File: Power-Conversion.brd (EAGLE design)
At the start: 182.9 x 114.3 mm, 50 parts, among them Q1 SUM90P10-19L, U7 LM2678

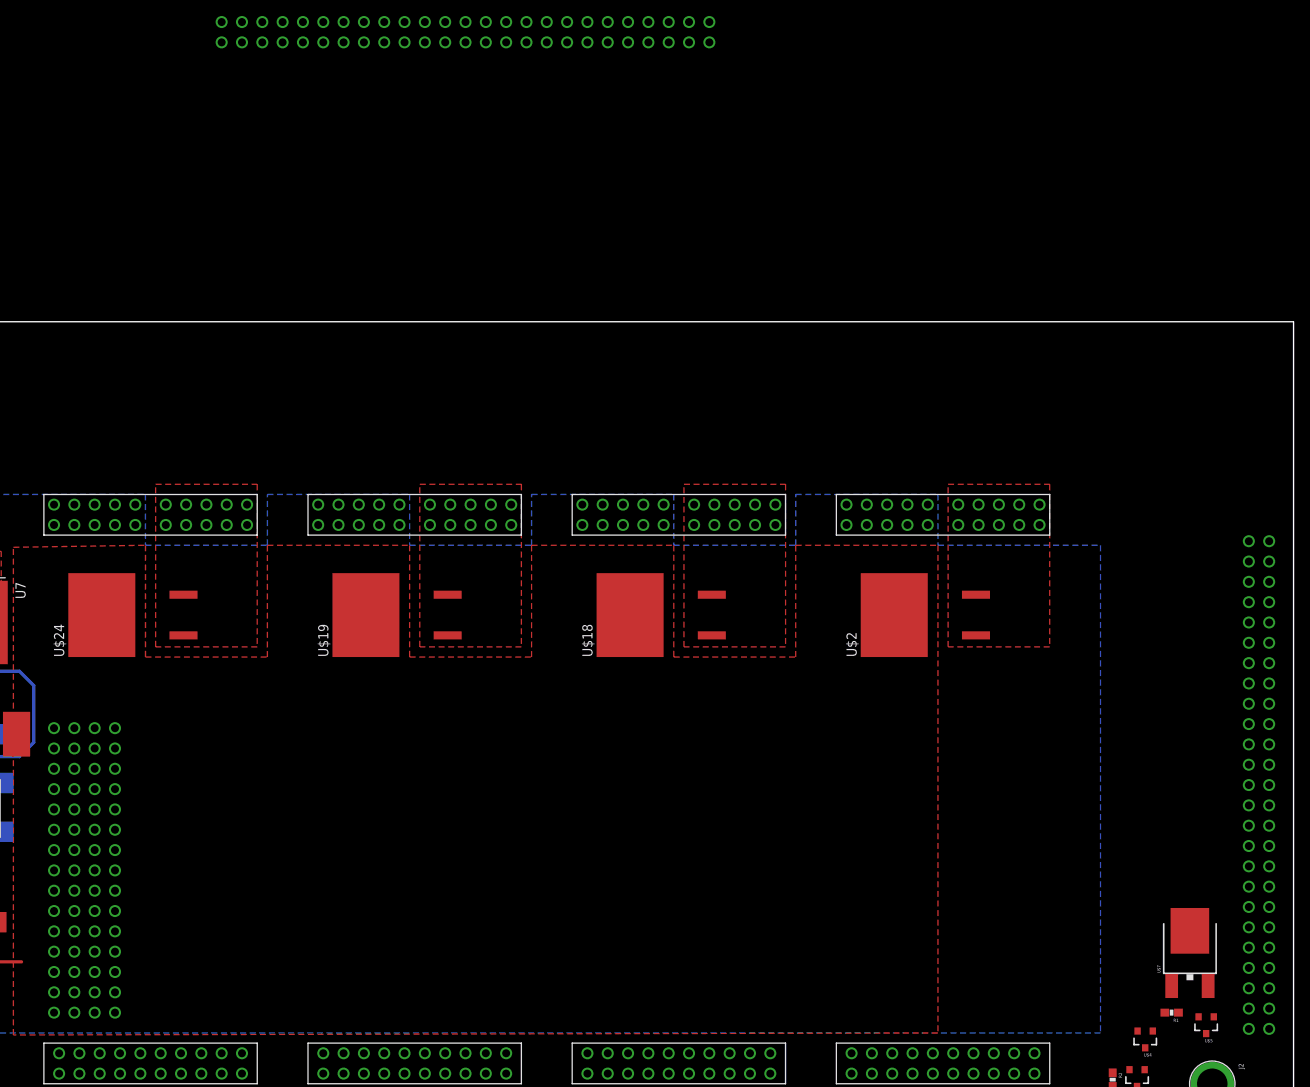
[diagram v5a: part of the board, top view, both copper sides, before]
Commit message: Added standard ESC board connector
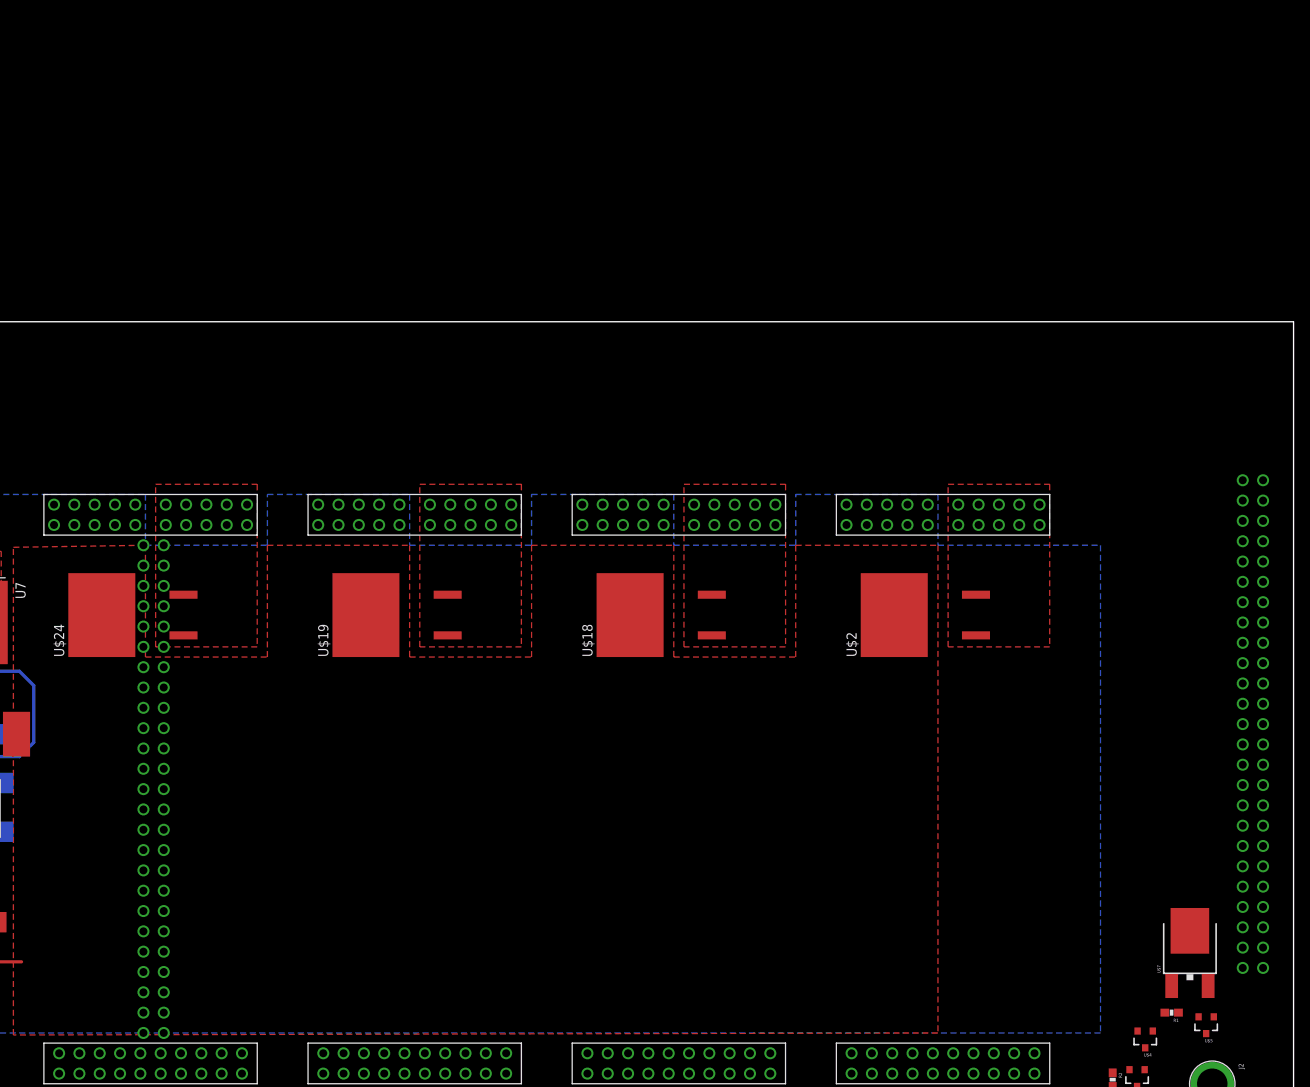
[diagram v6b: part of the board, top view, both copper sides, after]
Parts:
- removed U$13, U$14: POWER_BRICK_CONNECTORS(2X15), MotherBoardParts2:POWER_BRICK_CONNECTORS(2X15)
- removed U$3, U$8: POWER-BRICK-CONNECTOR, MotherboardParts:POWER-BRICK-CONNECTOR
- added U$17: ESC-CONNECTORESC-CONNECTOR, MotherboardParts:ESC-CONNECTOR
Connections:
- net +12V: now also U$17.P$100, U$17.P$51, U$17.P$52, U$17.P$53, U$17.P$54, U$17.P$55, U$17.P$56, U$17.P$57, U$17.P$58, U$17.P$59, U$17.P$60, U$17.P$61, U$17.P$62, U$17.P$63, U$17.P$64, U$17.P$65, U$17.P$66, U$17.P$67, U$17.P$68, U$17.P$69, U$17.P$70, U$17.P$71, U$17.P$72, U$17.P$73, U$17.P$74, U$17.P$75, U$17.P$76, U$17.P$77, U$17.P$78, U$17.P$79, U$17.P$80, U$17.P$81, U$17.P$82, U$17.P$83, U$17.P$84, U$17.P$85, U$17.P$86, U$17.P$87, U$17.P$88, U$17.P$89, U$17.P$90, U$17.P$91, U$17.P$92, U$17.P$93, U$17.P$94, U$17.P$95, U$17.P$96, U$17.P$97, U$17.P$98, U$17.P$99; no longer U$8.P$1, U$8.P$10, U$8.P$11, U$8.P$12, U$8.P$13, U$8.P$14, U$8.P$15, U$8.P$16, U$8.P$17, U$8.P$18, U$8.P$19, U$8.P$2, U$8.P$20, U$8.P$21, U$8.P$22, U$8.P$23, U$8.P$24, U$8.P$25, U$8.P$26, U$8.P$27, U$8.P$28, U$8.P$29, U$8.P$3, U$8.P$30, U$8.P$31, U$8.P$32, U$8.P$33, U$8.P$34, U$8.P$35, U$8.P$36, U$8.P$37, U$8.P$38, U$8.P$39, U$8.P$4, U$8.P$40, U$8.P$41, U$8.P$42, U$8.P$43, U$8.P$44, U$8.P$45, U$8.P$46, U$8.P$47, U$8.P$48, U$8.P$49, U$8.P$5, U$8.P$50, U$8.P$6, U$8.P$7, U$8.P$8, U$8.P$9
- net GND: now also U$17.P$1, U$17.P$10, U$17.P$11, U$17.P$12, U$17.P$13, U$17.P$14, U$17.P$15, U$17.P$16, U$17.P$17, U$17.P$18, U$17.P$19, U$17.P$2, U$17.P$20, U$17.P$21, U$17.P$22, U$17.P$23, U$17.P$24, U$17.P$25, U$17.P$26, U$17.P$27, U$17.P$28, U$17.P$29, U$17.P$3, U$17.P$30, U$17.P$31, U$17.P$32, U$17.P$33, U$17.P$34, U$17.P$35, U$17.P$36, U$17.P$37, U$17.P$38, U$17.P$39, U$17.P$4, U$17.P$40, U$17.P$41, U$17.P$42, U$17.P$43, U$17.P$44, U$17.P$45, U$17.P$46, U$17.P$47, U$17.P$48, U$17.P$49, U$17.P$5, U$17.P$50, U$17.P$6, U$17.P$7, U$17.P$8, U$17.P$9; no longer U$3.P$1, U$3.P$10, U$3.P$11, U$3.P$12, U$3.P$13, U$3.P$14, U$3.P$15, U$3.P$16, U$3.P$17, U$3.P$18, U$3.P$19, U$3.P$2, U$3.P$20, U$3.P$21, U$3.P$22, U$3.P$23, U$3.P$24, U$3.P$25, U$3.P$26, U$3.P$27, U$3.P$28, U$3.P$29, U$3.P$3, U$3.P$30, U$3.P$31, U$3.P$32, U$3.P$33, U$3.P$34, U$3.P$35, U$3.P$36, U$3.P$37, U$3.P$38, U$3.P$39, U$3.P$4, U$3.P$40, U$3.P$41, U$3.P$42, U$3.P$43, U$3.P$44, U$3.P$45, U$3.P$46, U$3.P$47, U$3.P$48, U$3.P$49, U$3.P$5, U$3.P$50, U$3.P$6, U$3.P$7, U$3.P$8, U$3.P$9

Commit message: Some routing done
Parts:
- U$17: value ESC-CONNECTORESC-CONNECTOR -> ESC-CONNECTORPARALLELL; device MotherboardParts:ESC-CONNECTOR -> MotherboardParts:ESC-PARALLELL
- turned R5 to 180 degrees
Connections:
- removed net SCL4: U$23.SCL
- removed net SDA4: U$23.SDA
- net +12V: now also U$17.P$101, U$17.P$102, U$17.P$103, U$17.P$104, U$17.P$105, U$17.P$106, U$17.P$107, U$17.P$108, U$17.P$109, U$17.P$110, U$17.P$111, U$17.P$112, U$17.P$113, U$17.P$114, U$17.P$115, U$17.P$116, U$17.P$117, U$17.P$118, U$17.P$119, U$17.P$120, U$17.P$121, U$17.P$122, U$17.P$123, U$17.P$124, U$17.P$125, U$17.P$126, U$17.P$127, U$17.P$128, U$17.P$129, U$17.P$130; no longer U$17.P$100, U$17.P$81, U$17.P$82, U$17.P$83, U$17.P$84, U$17.P$85, U$17.P$86, U$17.P$87, U$17.P$88, U$17.P$89, U$17.P$90, U$17.P$91, U$17.P$92, U$17.P$93, U$17.P$94, U$17.P$95, U$17.P$96, U$17.P$97, U$17.P$98, U$17.P$99
- net SCL1: now also U$23.SCL
- net SDA1: now also U$23.SDA
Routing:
- net GND: track 19.7 -> 33.1 mm
- net SDA: track 0.00 -> 5.31 mm
- net SCL: track 0.00 -> 5.29 mm

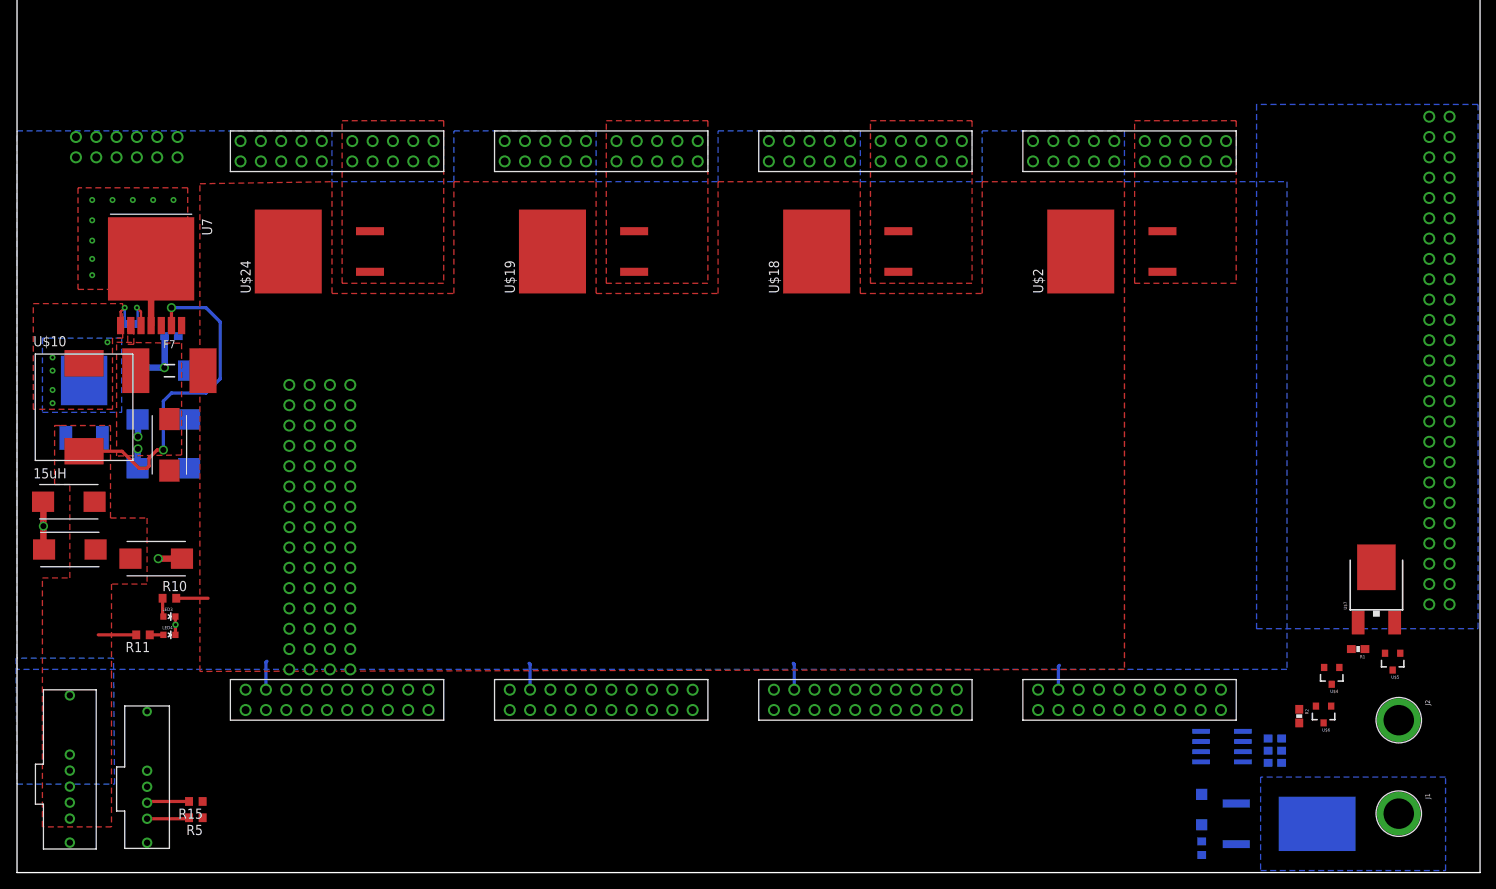
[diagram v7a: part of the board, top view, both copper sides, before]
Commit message: finished board layout
first draft board layout
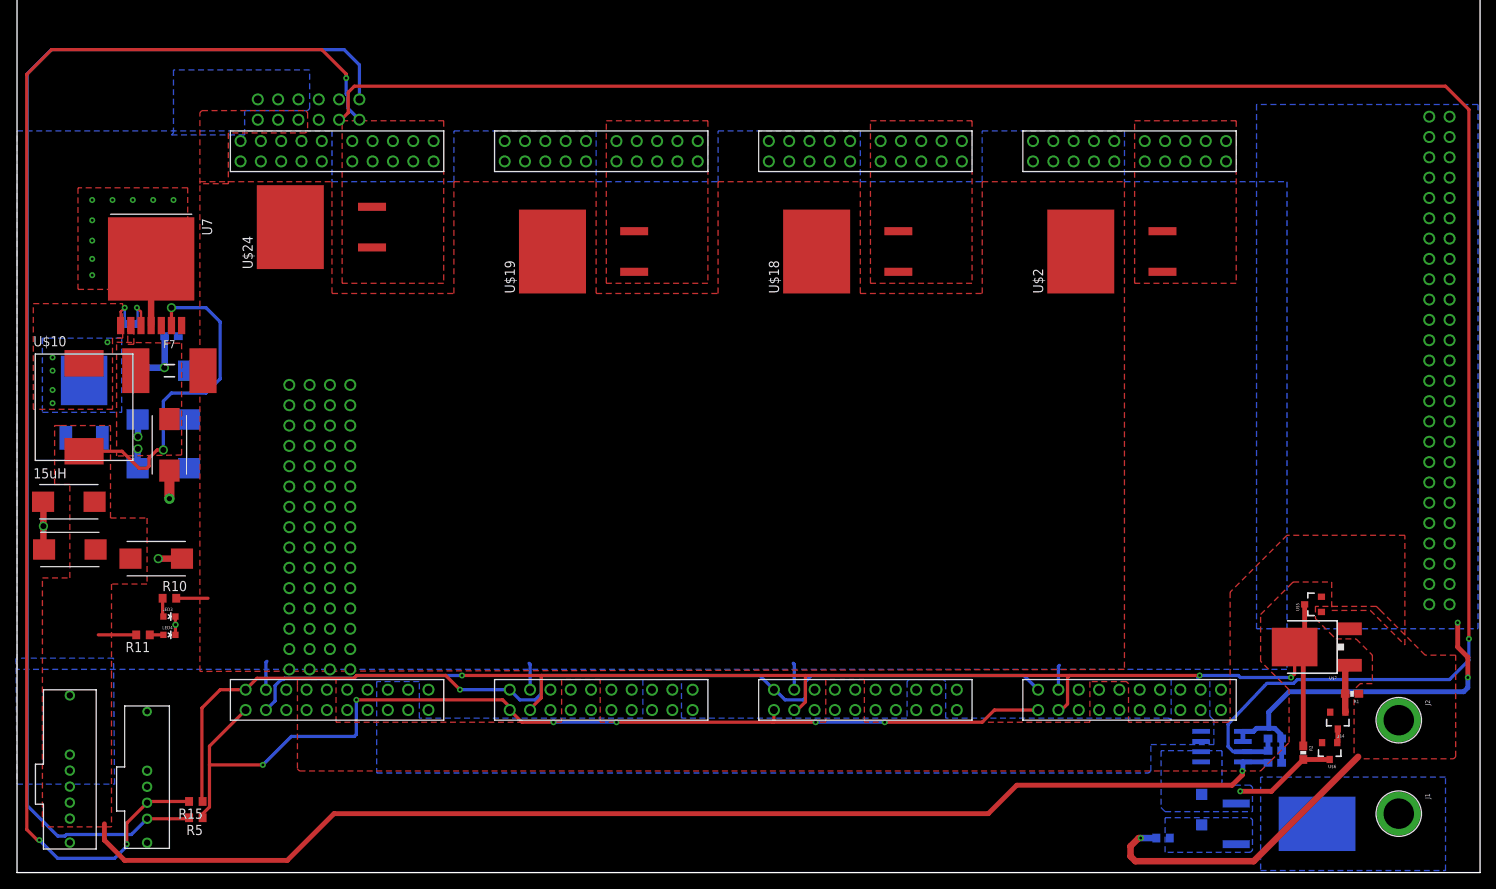
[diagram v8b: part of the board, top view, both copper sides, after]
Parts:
- moved U$16 23.2 mm to (36.4, 95.4)
- moved U$5 12.2 mm to (162.1, 33.5), turned to 90 degrees
- moved U$7 12.0 mm to (161.3, 28.2), turned to 90 degrees
- moved R1 5.64 mm to (166.9, 22.4)
- moved U$4 5.64 mm to (165.1, 19.1)
- moved R3 4.99 mm to (143.3, 4.32), turned to 180 degrees
- moved U$6 4.64 mm to (164.1, 15.2)
- moved R2 4.60 mm to (160.8, 15.0)
- moved U$24 3.06 mm to (38.4, 75.4)
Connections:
- removed net ONOFF: R2.1, U$5.3, U$7.4
- removed net V-: U$20.48V_GND1, U$20.48V_GND2, U$20.48V_GND3, U$20.48V_GND4, U$21.48V_GND1, U$21.48V_GND2, U$21.48V_GND3, U$21.48V_GND4, U$22.48V_GND1, U$22.48V_GND2, U$22.48V_GND3, U$22.48V_GND4, U$23.48V_GND1, U$23.48V_GND2, U$23.48V_GND3, U$23.48V_GND4
- net 48V_GND: now also U$20.48V_GND1, U$20.48V_GND2, U$20.48V_GND3, U$20.48V_GND4, U$21.48V_GND1, U$21.48V_GND2, U$21.48V_GND3, U$21.48V_GND4, U$22.48V_GND1, U$22.48V_GND2, U$22.48V_GND3, U$22.48V_GND4, U$23.48V_GND1, U$23.48V_GND2, U$23.48V_GND3, U$23.48V_GND4
- net ON/OFF: now also R2.1, U$5.3, U$7.4
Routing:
- net 48_I_ANALOG: track 0.00 -> 257.7 mm, vias 0 -> 1
- net ON/OFF: track 0.00 -> 169.5 mm, vias 0 -> 3
- net SDA: track 5.31 -> 169.7 mm, vias 0 -> 3
- net SCL: track 5.29 -> 162.1 mm
- net +5V: track 47.6 -> 202.3 mm, vias 2 -> 3
- net SCL1: track 0.00 -> 128.7 mm, vias 0 -> 6
- net SDA1: track 0.00 -> 126.2 mm, vias 0 -> 1
- net GND: track 33.1 -> 83.5 mm, vias 12 -> 15
- net 48V_GND: track 0.00 -> 39.0 mm, vias 0 -> 1
- net +48V: track 0.00 -> 12.8 mm, vias 0 -> 1
- net N$10: track 0.00 -> 6.11 mm
- net N$9: track 0.00 -> 1.74 mm
- added copper zone on layer 16, net +48V
- added copper zone on layer 1, net 48V_GND
- added copper zone on layer 16, net N$5
- added copper zone on layer 16, net VCC
